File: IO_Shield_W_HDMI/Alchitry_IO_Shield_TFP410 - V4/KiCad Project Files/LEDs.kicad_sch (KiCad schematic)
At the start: 55 parts, among them Q1 Q_PMOS_SGD, Q2 Q_PMOS_SGD, Q3 Q_PMOS_SGD, Q4 Q_PMOS_SGD, SW1 SW_DIP_x08, SW2 SW_DIP_x08, SW3 SW_DIP_x08

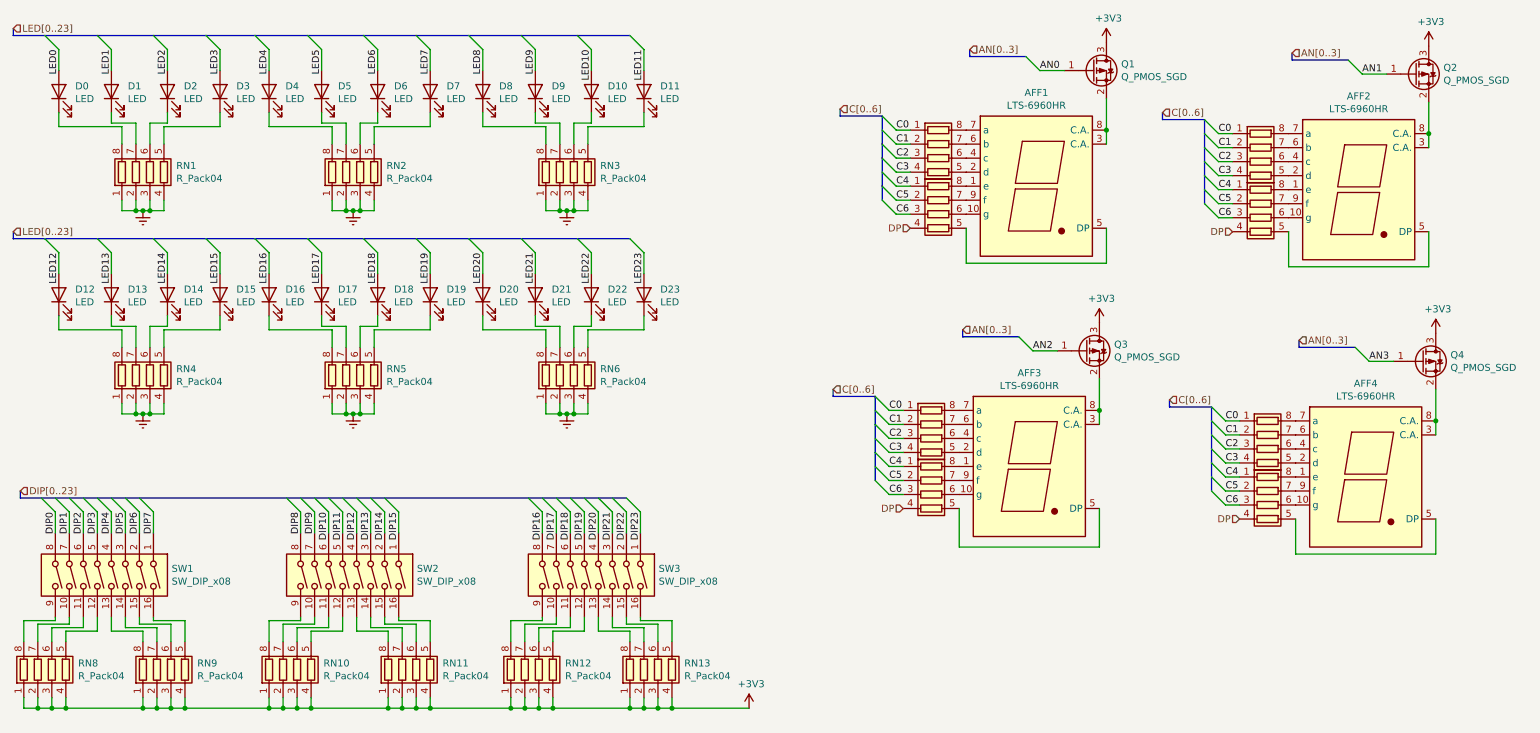
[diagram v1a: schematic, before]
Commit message: updated shield v4 schematic
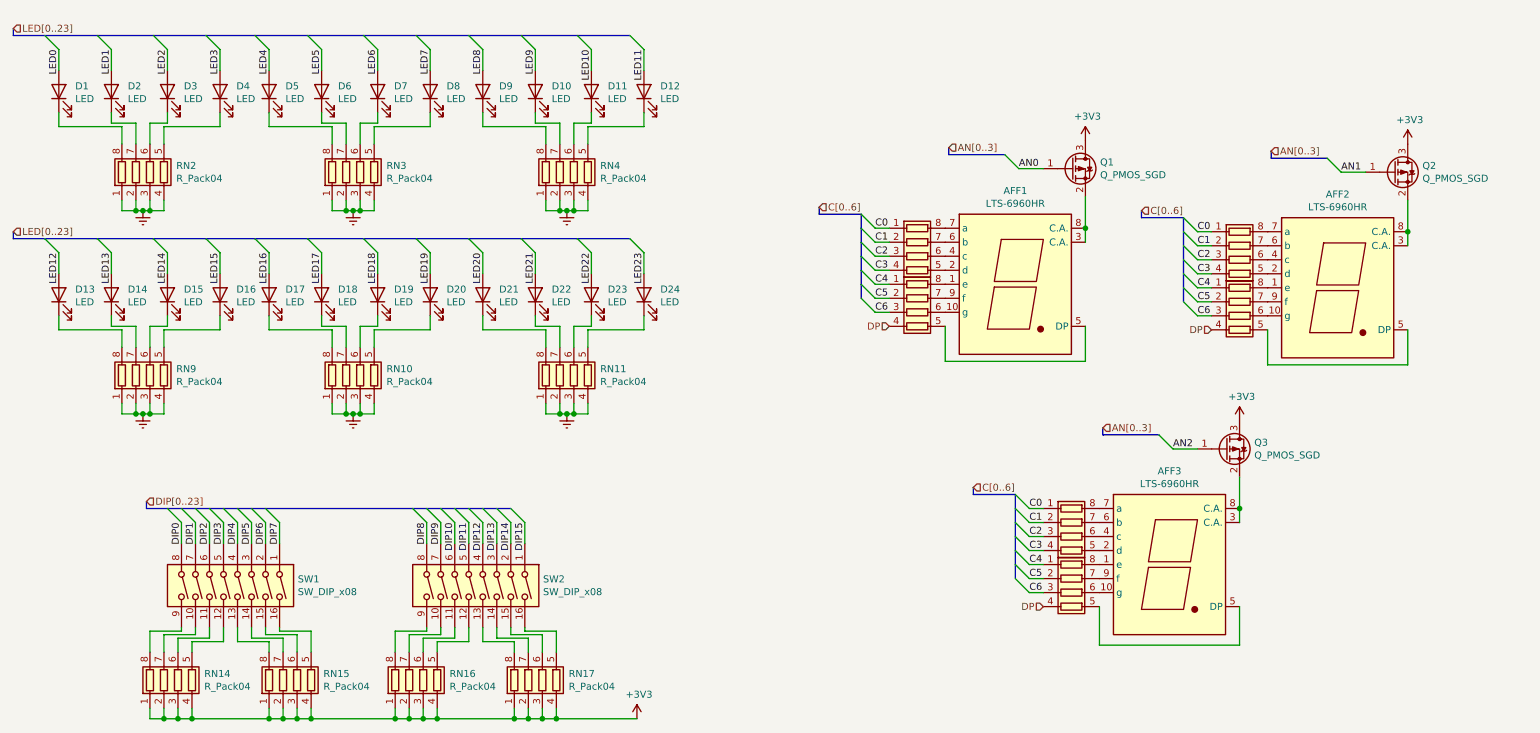
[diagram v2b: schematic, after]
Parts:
- removed AFF4: LTS-6960HR, Display_7Segment:KCSC02-136, symbol Display_Character:LTS-6960HR
- removed Q4: Q_PMOS_SGD, Package_TO_SOT_SMD:SOT-23, symbol Device:Q_PMOS_GSD
- removed RN12, RN13, RN19, RN21: R_Pack04, Resistor_SMD:R_Array_Convex_4x0603, symbol Device:R_Pack04
- removed SW3: SW_DIP_x08, Button_Switch_SMD:SW_DIP_SPSTx08_Slide_Copal_CHS-08B_W7.62mm_P1.27mm, symbol Switch:SW_DIP_x08
- D1: renamed from D0; footprint LED_SMD:LED_0603_1608Metric_Pad1.05x0.95mm_HandSolder -> LED_SMD:LED_0603_1608Metric
- D10: renamed from D9; footprint LED_SMD:LED_0603_1608Metric_Pad1.05x0.95mm_HandSolder -> LED_SMD:LED_0603_1608Metric
- D11: renamed from D10; footprint LED_SMD:LED_0603_1608Metric_Pad1.05x0.95mm_HandSolder -> LED_SMD:LED_0603_1608Metric
- D12: renamed from D11; footprint LED_SMD:LED_0603_1608Metric_Pad1.05x0.95mm_HandSolder -> LED_SMD:LED_0603_1608Metric
- D13: renamed from D12; footprint LED_SMD:LED_0603_1608Metric_Pad1.05x0.95mm_HandSolder -> LED_SMD:LED_0603_1608Metric
- D14: renamed from D13; footprint LED_SMD:LED_0603_1608Metric_Pad1.05x0.95mm_HandSolder -> LED_SMD:LED_0603_1608Metric
- D15: renamed from D14; footprint LED_SMD:LED_0603_1608Metric_Pad1.05x0.95mm_HandSolder -> LED_SMD:LED_0603_1608Metric
- D16: renamed from D15; footprint LED_SMD:LED_0603_1608Metric_Pad1.05x0.95mm_HandSolder -> LED_SMD:LED_0603_1608Metric
- D17: renamed from D16; footprint LED_SMD:LED_0603_1608Metric_Pad1.05x0.95mm_HandSolder -> LED_SMD:LED_0603_1608Metric
- D18: renamed from D17; footprint LED_SMD:LED_0603_1608Metric_Pad1.05x0.95mm_HandSolder -> LED_SMD:LED_0603_1608Metric
- D19: renamed from D18; footprint LED_SMD:LED_0603_1608Metric_Pad1.05x0.95mm_HandSolder -> LED_SMD:LED_0603_1608Metric
- D2: renamed from D1; footprint LED_SMD:LED_0603_1608Metric_Pad1.05x0.95mm_HandSolder -> LED_SMD:LED_0603_1608Metric
- D20: renamed from D19; footprint LED_SMD:LED_0603_1608Metric_Pad1.05x0.95mm_HandSolder -> LED_SMD:LED_0603_1608Metric
- D21: renamed from D20; footprint LED_SMD:LED_0603_1608Metric_Pad1.05x0.95mm_HandSolder -> LED_SMD:LED_0603_1608Metric
- D22: renamed from D21; footprint LED_SMD:LED_0603_1608Metric_Pad1.05x0.95mm_HandSolder -> LED_SMD:LED_0603_1608Metric
- D23: renamed from D22; footprint LED_SMD:LED_0603_1608Metric_Pad1.05x0.95mm_HandSolder -> LED_SMD:LED_0603_1608Metric
- D24: renamed from D23; footprint LED_SMD:LED_0603_1608Metric_Pad1.05x0.95mm_HandSolder -> LED_SMD:LED_0603_1608Metric
- D3: renamed from D2; footprint LED_SMD:LED_0603_1608Metric_Pad1.05x0.95mm_HandSolder -> LED_SMD:LED_0603_1608Metric
- D4: renamed from D3; footprint LED_SMD:LED_0603_1608Metric_Pad1.05x0.95mm_HandSolder -> LED_SMD:LED_0603_1608Metric
- D5: renamed from D4; footprint LED_SMD:LED_0603_1608Metric_Pad1.05x0.95mm_HandSolder -> LED_SMD:LED_0603_1608Metric
- D6: renamed from D5; footprint LED_SMD:LED_0603_1608Metric_Pad1.05x0.95mm_HandSolder -> LED_SMD:LED_0603_1608Metric
- D7: renamed from D6; footprint LED_SMD:LED_0603_1608Metric_Pad1.05x0.95mm_HandSolder -> LED_SMD:LED_0603_1608Metric
- D8: renamed from D7; footprint LED_SMD:LED_0603_1608Metric_Pad1.05x0.95mm_HandSolder -> LED_SMD:LED_0603_1608Metric
- D9: renamed from D8; footprint LED_SMD:LED_0603_1608Metric_Pad1.05x0.95mm_HandSolder -> LED_SMD:LED_0603_1608Metric
- renumbered RN5 to RN10, RN6 to RN11, RN18 to RN12, RN20 to RN13, RN8 to RN14, RN9 to RN15, RN10 to RN16, RN11 to RN17, RN1 to RN2, RN2 to RN3, RN3 to RN4, RN14 to RN5, RN15 to RN6, RN16 to RN7, RN17 to RN8, RN4 to RN9
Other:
- moved on the sheet: AFF1, AFF2, AFF3, Q1, Q2, Q3, RN14, RN15, RN16, RN17, SW1, SW2
